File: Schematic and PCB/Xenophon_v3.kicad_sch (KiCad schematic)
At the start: 36 parts, among them J1 USB_C_Receptacle_USB2.0, J2 AudioJack3, J3 USB_C_Receptacle_USB2.0, J4 AudioJack3, U1 ATmega32U4-A, U2 ATmega32U4-A, Y1 Crystal, Y2 Crystal

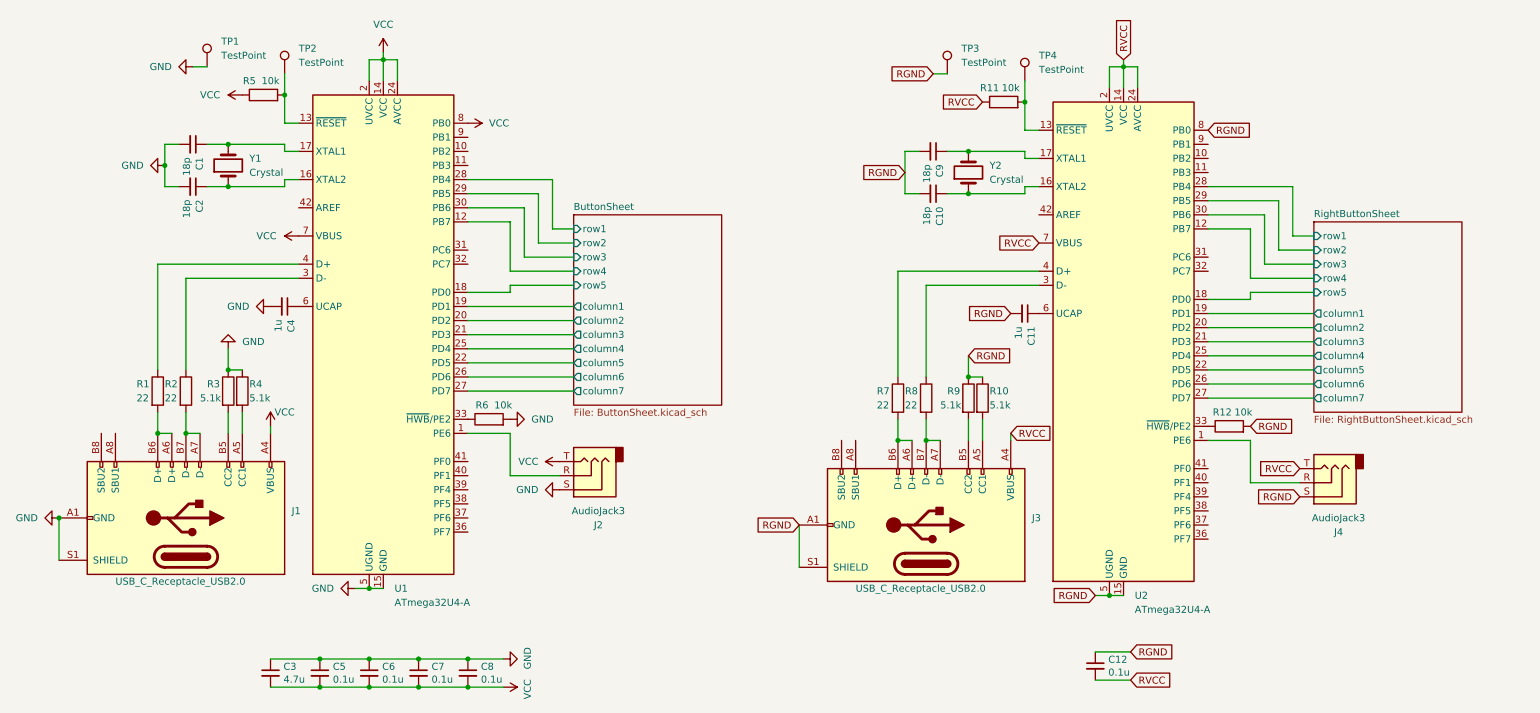
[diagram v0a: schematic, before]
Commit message: Panelized the pcb
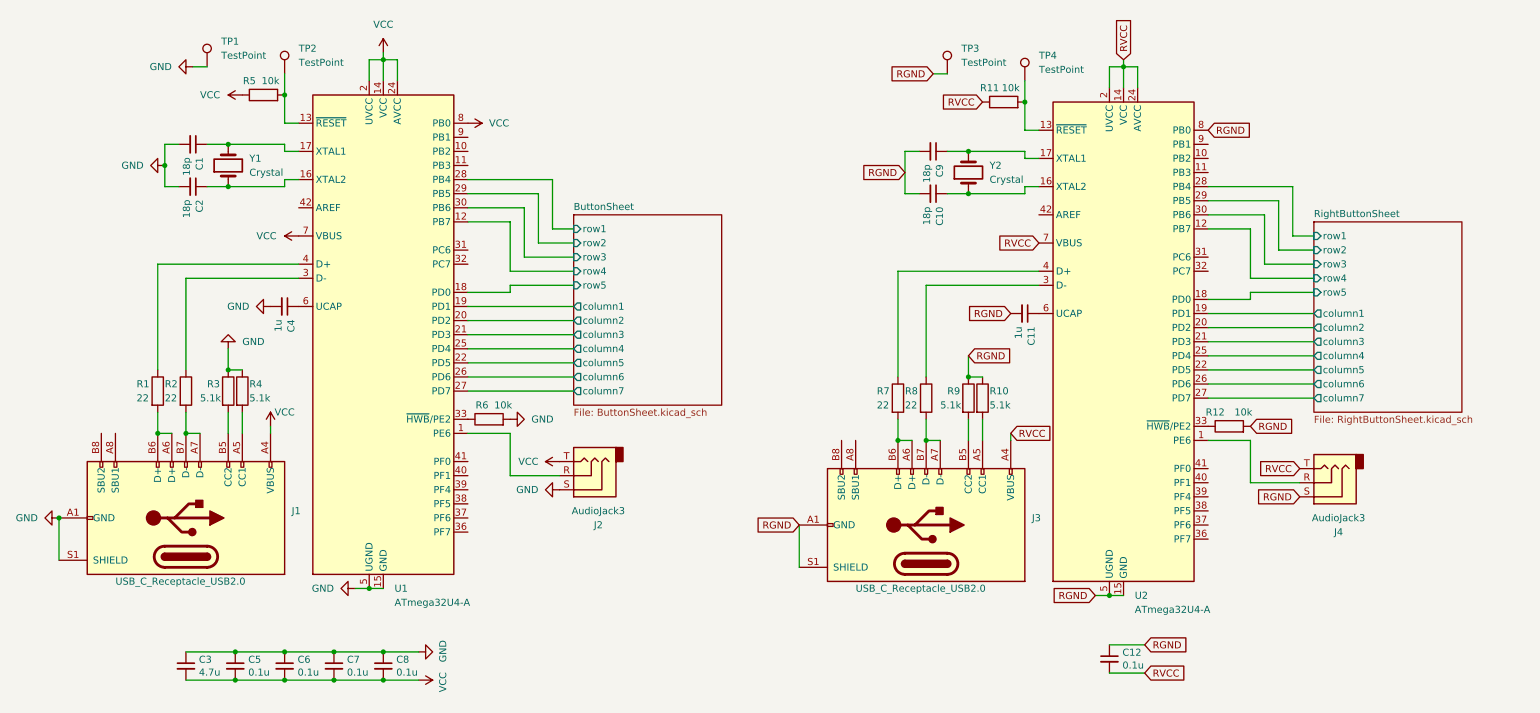
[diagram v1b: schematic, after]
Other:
- moved on the sheet: C12, C3, C5, C6, C7, C8
